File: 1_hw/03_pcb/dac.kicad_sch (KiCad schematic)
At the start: 6 parts, among them U7 AD9744

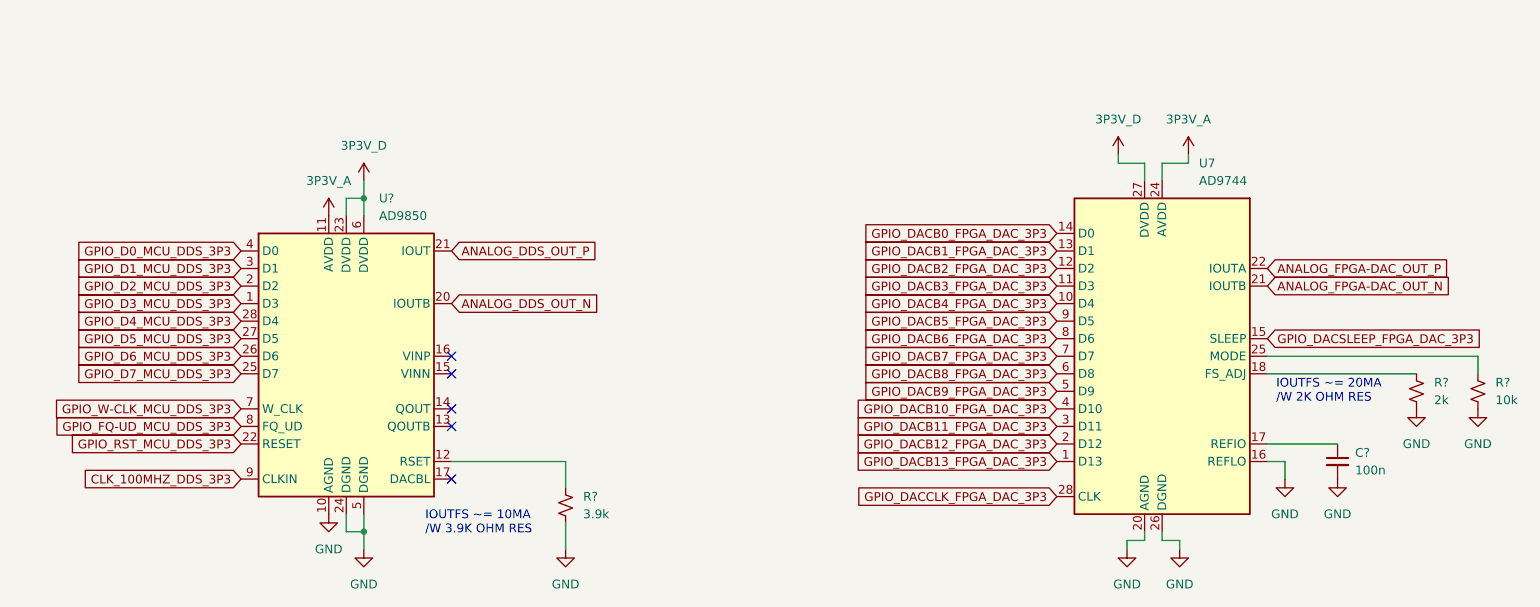
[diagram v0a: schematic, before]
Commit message: FEAT: Added Connectors on Schematic. Created Connector Footprints.
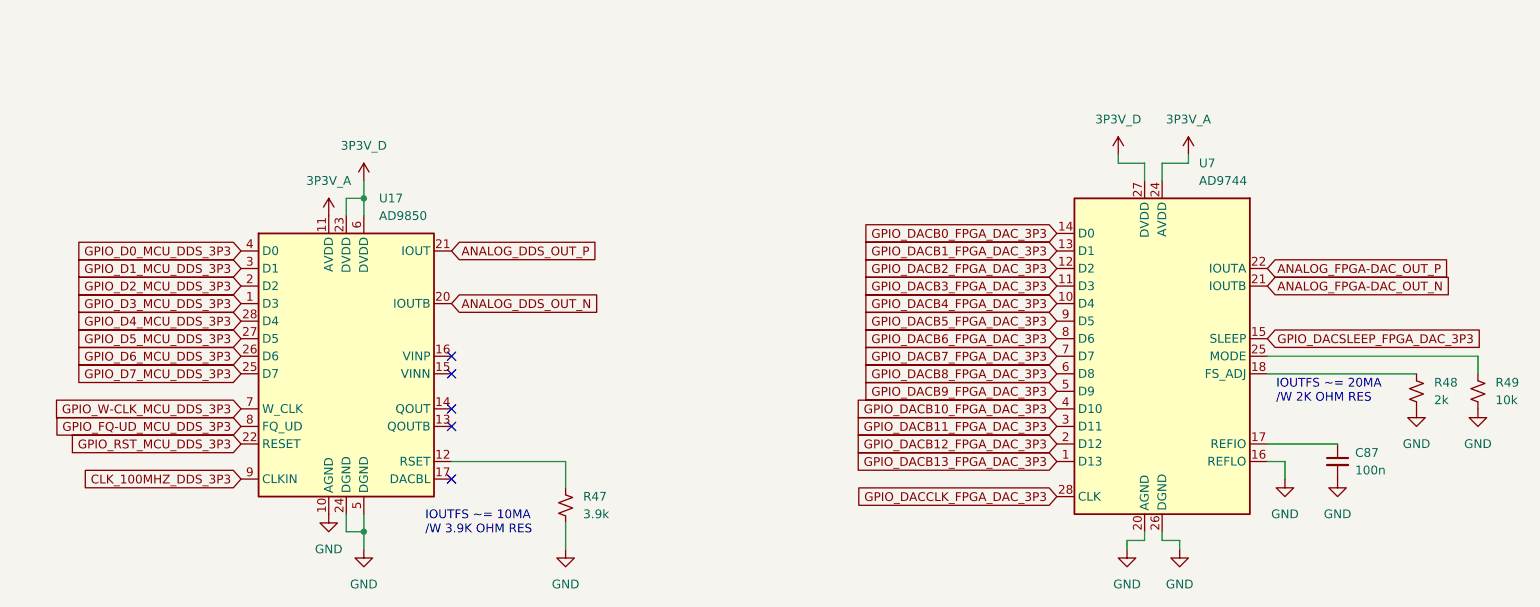
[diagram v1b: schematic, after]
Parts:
- gave numbers to parts that had none: 5
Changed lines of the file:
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@@
 		(dnp no)
 		(fields_autoplaced yes)
-		(property "Reference" "U?"
+		(property "Reference" "U17"
 			(at 96.1741 63.5 0)
 			(effects
@@
 			(project ""
 				(path "/866ef9be-3b01-4288-a6e0-a2357aa17e50/7126ceca-2dec-4994-855f-f217c0acdc71"
-					(reference "U?")
+					(reference "U17")
 					(unit 1)
 				)
@@
 		(dnp no)
 		(fields_autoplaced yes)
-		(property "Reference" "R?"
+		(property "Reference" "R47"
 			(at 125.73 106.6799 0)
 			(effects
@@
 			(project "arb"
 				(path "/866ef9be-3b01-4288-a6e0-a2357aa17e50/7126ceca-2dec-4994-855f-f217c0acdc71"
-					(reference "R?")
+					(reference "R47")
 					(unit 1)
 				)
@@
 		(dnp no)
 		(fields_autoplaced yes)
-		(property "Reference" "R?"
+		(property "Reference" "R49"
 			(at 257.81 90.1699 0)
 			(effects
@@
 			(project "arb"
 				(path "/866ef9be-3b01-4288-a6e0-a2357aa17e50/7126ceca-2dec-4994-855f-f217c0acdc71"
-					(reference "R?")
+					(reference "R49")
 					(unit 1)
 				)
@@
 		(dnp no)
 		(fields_autoplaced yes)
-		(property "Reference" "R?"
+		(property "Reference" "R48"
 			(at 248.92 90.1699 0)
 			(effects
@@
 			(project "arb"
 				(path "/866ef9be-3b01-4288-a6e0-a2357aa17e50/7126ceca-2dec-4994-855f-f217c0acdc71"
-					(reference "R?")
+					(reference "R48")
 					(unit 1)
 				)
@@
 		(dnp no)
 		(fields_autoplaced yes)
-		(property "Reference" "C?"
+		(property "Reference" "C87"
 			(at 237.49 100.3363 0)
 			(effects
@@
 			(project "arb"
 				(path "/866ef9be-3b01-4288-a6e0-a2357aa17e50/7126ceca-2dec-4994-855f-f217c0acdc71"
-					(reference "C?")
-					(unit 1)
-				)
+					(reference "C87")
+					(unit 1)
+				)

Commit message: FEAT: Assigned Reference Designators; Assigned Passives Part Numbers & Footprints (0603); Assigned LCSC P/Ns.
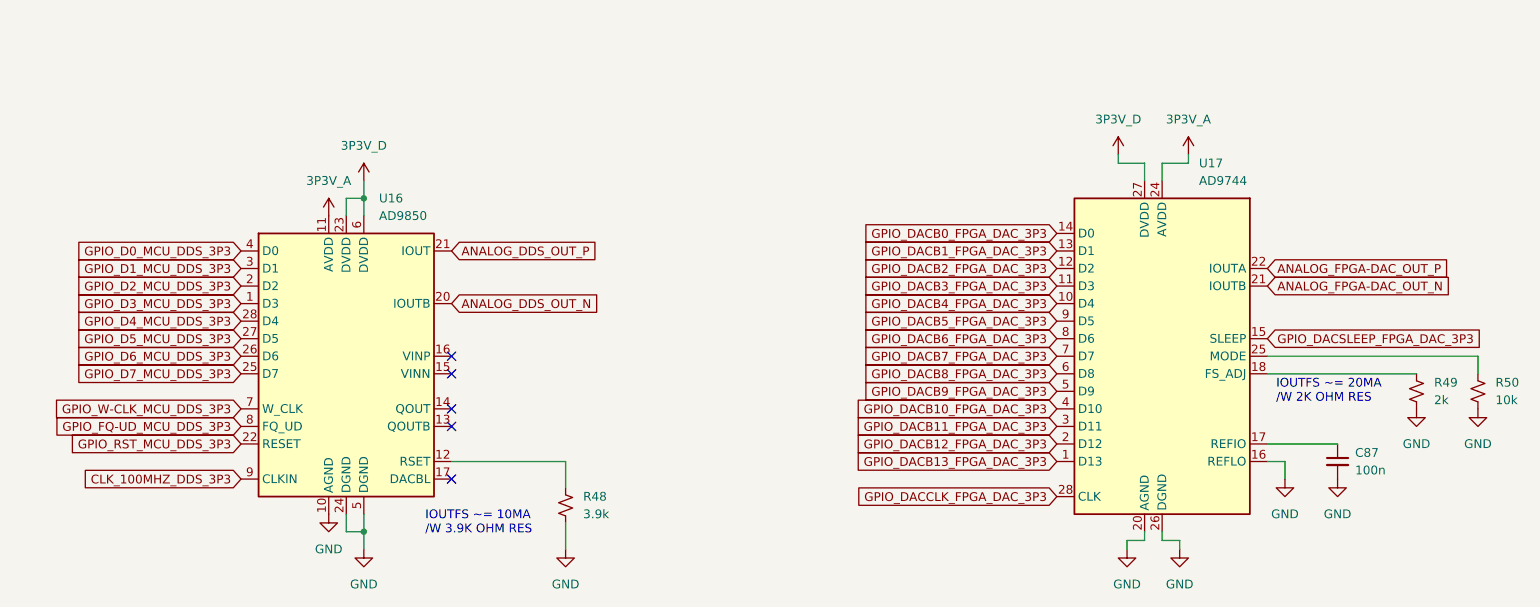
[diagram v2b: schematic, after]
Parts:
- C87: LCSC (none) -> C24452; PN CL10B104JB8NNNC -> (none); Part Number (none) -> CL10B104JB8NNNC
- R48: renamed from R47; LCSC (none) -> C23018; PN tbd -> (none); Part Number (none) -> 0603WAF3901T5E
- R49: renamed from R48; LCSC (none) -> C22975; PN tbd -> (none); Part Number (none) -> 0603WAF2001T5E
- R50: renamed from R49; LCSC (none) -> C25804; PN CR-03FC7---10K -> (none); Part Number (none) -> 0603WAF1002T5E
- U16: renamed from U17; LCSC (none) -> C18731; Part Number (none) -> AD9850BRSZ
- U17: renamed from U7; LCSC (none) -> C461519
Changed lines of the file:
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@@
 		(dnp no)
 		(fields_autoplaced yes)
-		(property "Reference" "#PWR097"
+		(property "Reference" "#PWR0202"
 			(at 204.47 120.65 0)
 			(effects
@@
 			(project "arb"
 				(path "/866ef9be-3b01-4288-a6e0-a2357aa17e50/7126ceca-2dec-4994-855f-f217c0acdc71"
-					(reference "#PWR097")
+					(reference "#PWR0202")
 					(unit 1)
 				)
@@
 		(dnp no)
 		(fields_autoplaced yes)
-		(property "Reference" "#PWR0100"
+		(property "Reference" "#PWR0206"
 			(at 234.95 110.49 0)
 			(effects
@@
 			(project "arb"
 				(path "/866ef9be-3b01-4288-a6e0-a2357aa17e50/7126ceca-2dec-4994-855f-f217c0acdc71"
-					(reference "#PWR0100")
+					(reference "#PWR0206")
 					(unit 1)
 				)
@@
 		(dnp no)
 		(fields_autoplaced yes)
-		(property "Reference" "#PWR098"
+		(property "Reference" "#PWR0203"
 			(at 212.09 120.65 0)
 			(effects
@@
 			(project "arb"
 				(path "/866ef9be-3b01-4288-a6e0-a2357aa17e50/7126ceca-2dec-4994-855f-f217c0acdc71"
-					(reference "#PWR098")
+					(reference "#PWR0203")
 					(unit 1)
 				)
@@
 		(dnp no)
 		(fields_autoplaced yes)
-		(property "Reference" "U17"
+		(property "Reference" "U16"
 			(at 96.1741 63.5 0)
 			(effects
@@
 			)
 		)
+		(property "LCSC" "C18731"
+			(at 91.44 86.36 0)
+			(effects
+				(font
+					(size 1.27 1.27)
+				)
+				(hide yes)
+			)
+		)
+		(property "Part Number" "AD9850BRSZ"
+			(at 91.44 86.36 0)
+			(effects
+				(font
+					(size 1.27 1.27)
+				)
+				(hide yes)
+			)
+		)
 		(pin "26"
 		)
@@
 			(project ""
 				(path "/866ef9be-3b01-4288-a6e0-a2357aa17e50/7126ceca-2dec-4994-855f-f217c0acdc71"
-					(reference "U17")
+					(reference "U16")
 					(unit 1)
 				)
@@
 		(dnp no)
 		(fields_autoplaced yes)
-		(property "Reference" "#PWR0156"
+		(property "Reference" "#PWR0198"
 			(at 93.98 64.77 0)
 			(effects
@@
 			(project "arb"
 				(path "/866ef9be-3b01-4288-a6e0-a2357aa17e50/7126ceca-2dec-4994-855f-f217c0acdc71"
-					(reference "#PWR0156")
+					(reference "#PWR0198")
 					(unit 1)
 				)
@@
 		(dnp no)
 		(fields_autoplaced yes)
-		(property "Reference" "#PWR0158"
+		(property "Reference" "#PWR0200"
 			(at 123.19 120.65 0)
 			(effects
@@
 			(project "arb"
 				(path "/866ef9be-3b01-4288-a6e0-a2357aa17e50/7126ceca-2dec-4994-855f-f217c0acdc71"
-					(reference "#PWR0158")
+					(reference "#PWR0200")
 					(unit 1)
 				)
@@
 		(dnp no)
 		(fields_autoplaced yes)
-		(property "Reference" "R47"
+		(property "Reference" "R48"
 			(at 125.73 106.6799 0)
 			(effects
@@
 			)
 		)
-		(property "PN" "tbd"
-			(at 123.19 107.95 90)
+		(property "LCSC" "C23018"
+			(at 123.19 107.95 0)
+			(effects
+				(font
+					(size 1.27 1.27)
+				)
+				(hide yes)
+			)
+		)
+		(property "Part Number" "0603WAF3901T5E"
+			(at 123.19 107.95 0)
 			(effects
 				(font
@@
 			(project "arb"
 				(path "/866ef9be-3b01-4288-a6e0-a2357aa17e50/7126ceca-2dec-4994-855f-f217c0acdc71"
-					(reference "R47")
+					(reference "R48")
 					(unit 1)
 				)
@@
 		(dnp no)
 		(fields_autoplaced yes)
-		(property "Reference" "R49"
+		(property "Reference" "R50"
 			(at 257.81 90.1699 0)
 			(effects
@@
 			)
 		)
-		(property "PN" "CR-03FC7---10K"
-			(at 255.27 91.44 90)
+		(property "Part Number" "0603WAF1002T5E"
+			(at 255.27 91.44 0)
+			(effects
+				(font
+					(size 1.27 1.27)
+				)
+				(hide yes)
+			)
+		)
+		(property "LCSC" "C25804"
+			(at 255.27 91.44 0)
 			(effects
 				(font
@@
 			(project "arb"
 				(path "/866ef9be-3b01-4288-a6e0-a2357aa17e50/7126ceca-2dec-4994-855f-f217c0acdc71"
-					(reference "R49")
+					(reference "R50")
 					(unit 1)
 				)
@@
 		(dnp no)
 		(fields_autoplaced yes)
-		(property "Reference" "#PWR096"
+		(property "Reference" "#PWR0204"
 			(at 213.36 60.96 0)
 			(effects
@@
 			(project "arb"
 				(path "/866ef9be-3b01-4288-a6e0-a2357aa17e50/7126ceca-2dec-4994-855f-f217c0acdc71"
-					(reference "#PWR096")
+					(reference "#PWR0204")
 					(unit 1)
 				)
@@
 		(dnp no)
 		(fields_autoplaced yes)
-		(property "Reference" "#PWR0159"
+		(property "Reference" "#PWR0199"
 			(at 93.98 120.65 0)
 			(effects
@@
 			(project "arb"
 				(path "/866ef9be-3b01-4288-a6e0-a2357aa17e50/7126ceca-2dec-4994-855f-f217c0acdc71"
-					(reference "#PWR0159")
+					(reference "#PWR0199")
 					(unit 1)
 				)
@@
 		(dnp no)
 		(fields_autoplaced yes)
-		(property "Reference" "#PWR099"
+		(property "Reference" "#PWR0208"
 			(at 255.27 100.33 0)
 			(effects
@@
 			(project "arb"
 				(path "/866ef9be-3b01-4288-a6e0-a2357aa17e50/7126ceca-2dec-4994-855f-f217c0acdc71"
-					(reference "#PWR099")
+					(reference "#PWR0208")
 					(unit 1)
 				)
@@
 		(dnp no)
 		(fields_autoplaced yes)
-		(property "Reference" "R48"
+		(property "Reference" "R49"
 			(at 248.92 90.1699 0)
 			(effects
@@
 			)
 		)
-		(property "PN" "tbd"
-			(at 246.38 91.44 90)
+		(property "LCSC" "C22975"
+			(at 246.38 91.44 0)
+			(effects
+				(font
+					(size 1.27 1.27)
+				)
+				(hide yes)
+			)
+		)
+		(property "Part Number" "0603WAF2001T5E"
+			(at 246.38 91.44 0)
 			(effects
 				(font
@@
 			(project "arb"
 				(path "/866ef9be-3b01-4288-a6e0-a2357aa17e50/7126ceca-2dec-4994-855f-f217c0acdc71"
-					(reference "R48")
+					(reference "R49")
 					(unit 1)
 				)
@@
 		(dnp no)
 		(fields_autoplaced yes)
-		(property "Reference" "#PWR0157"
+		(property "Reference" "#PWR0196"
 			(at 88.9 69.85 0)
 			(effects
@@
 			(project "arb"
 				(path "/866ef9be-3b01-4288-a6e0-a2357aa17e50/7126ceca-2dec-4994-855f-f217c0acdc71"
-					(reference "#PWR0157")
+					(reference "#PWR0196")
 					(unit 1)
 				)
@@
 		(dnp no)
 		(fields_autoplaced yes)
-		(property "Reference" "#PWR093"
+		(property "Reference" "#PWR0201"
 			(at 203.2 60.96 0)
 			(effects
@@
 			(project "arb"
 				(path "/866ef9be-3b01-4288-a6e0-a2357aa17e50/7126ceca-2dec-4994-855f-f217c0acdc71"
-					(reference "#PWR093")
+					(reference "#PWR0201")
 					(unit 1)
 				)
@@
 		(dnp no)
 		(fields_autoplaced yes)
-		(property "Reference" "#PWR0102"
+		(property "Reference" "#PWR0207"
 			(at 246.38 100.33 0)
 			(effects
@@
 			(project "arb"
 				(path "/866ef9be-3b01-4288-a6e0-a2357aa17e50/7126ceca-2dec-4994-855f-f217c0acdc71"
-					(reference "#PWR0102")
+					(reference "#PWR0207")
 					(unit 1)
 				)
@@
 		(dnp no)
 		(fields_autoplaced yes)
-		(property "Reference" "#PWR0160"
+		(property "Reference" "#PWR0197"
 			(at 88.9 115.57 0)
 			(effects
@@
 			(project "arb"
 				(path "/866ef9be-3b01-4288-a6e0-a2357aa17e50/7126ceca-2dec-4994-855f-f217c0acdc71"
-					(reference "#PWR0160")
+					(reference "#PWR0197")
 					(unit 1)
 				)
@@
 		(dnp no)
 		(fields_autoplaced yes)
-		(property "Reference" "#PWR0101"
+		(property "Reference" "#PWR0205"
 			(at 227.33 110.49 0)
 			(effects
@@
 			(project "arb"
 				(path "/866ef9be-3b01-4288-a6e0-a2357aa17e50/7126ceca-2dec-4994-855f-f217c0acdc71"
-					(reference "#PWR0101")
+					(reference "#PWR0205")
 					(unit 1)
 				)
@@
 			)
 		)
-		(property "PN" "CL10B104JB8NNNC"
+		(property "Part Number" "CL10B104JB8NNNC"
+			(at 234.95 101.6 0)
+			(effects
+				(font
+					(size 1.27 1.27)
+				)
+				(hide yes)
+			)
+		)
+		(property "LCSC" "C24452"
 			(at 234.95 101.6 0)
 			(effects
@@
 		(on_board yes)
 		(dnp no)
-		(property "Reference" "U7"
+		(property "Reference" "U17"
 			(at 214.884 58.42 0)
 			(effects
@@
 			)
 		)
+		(property "LCSC" "C461519"
+			(at 209.55 86.36 0)
+			(effects
+				(font
+					(size 1.27 1.27)
+				)
+				(hide yes)
+			)
+		)
 		(pin "28"
 		)
@@
 			(project ""
 				(path "/866ef9be-3b01-4288-a6e0-a2357aa17e50/7126ceca-2dec-4994-855f-f217c0acdc71"
-					(reference "U7")
-					(unit 1)
-				)
+					(reference "U17")
+					(unit 1)
+				)
